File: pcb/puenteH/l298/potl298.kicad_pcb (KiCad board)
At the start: 2 copper layers, 51.1 x 74.4 mm, 19 parts, among them K1 CONN_3, K2 CONN_3, P1 CONN_2X2, P2 v10, P3 CONN_2, P4 CONN_2, U1 L298

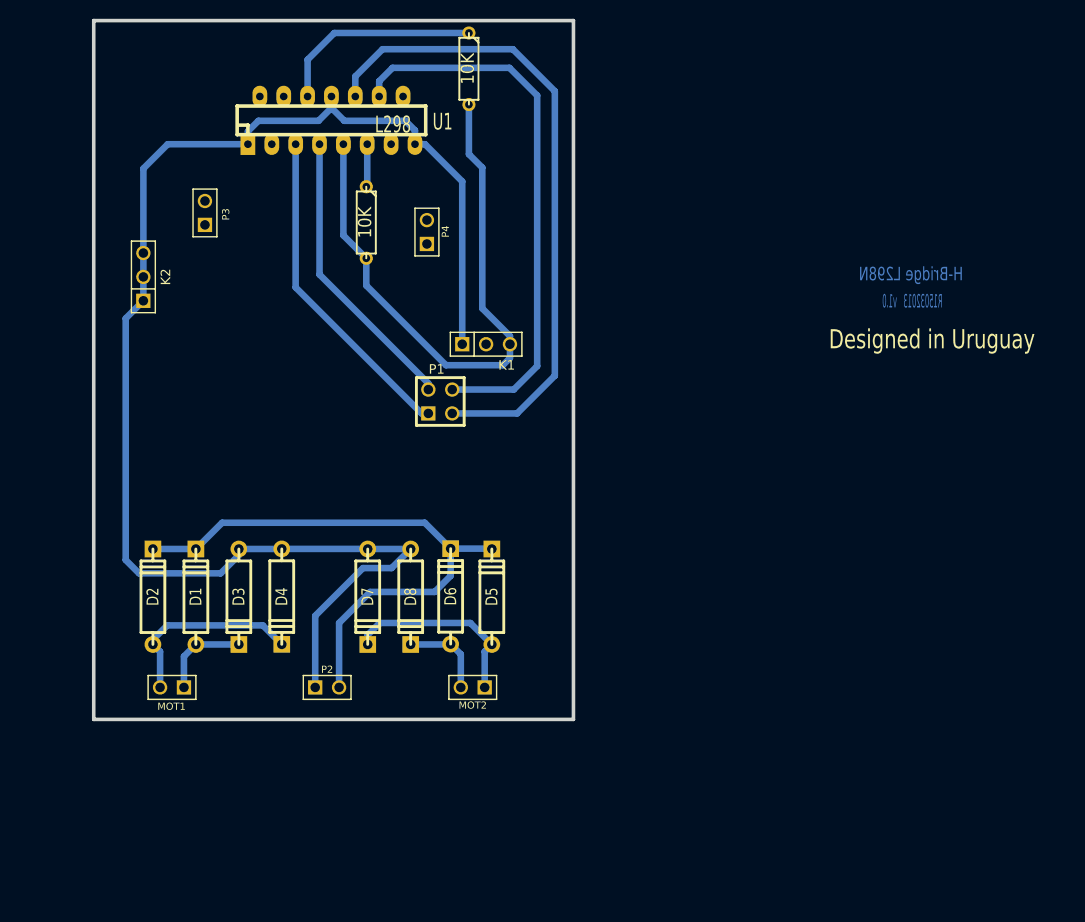
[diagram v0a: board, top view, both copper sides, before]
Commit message: H bridge L298 completed for connect to usb4butia (version 1.8.9 and futures)
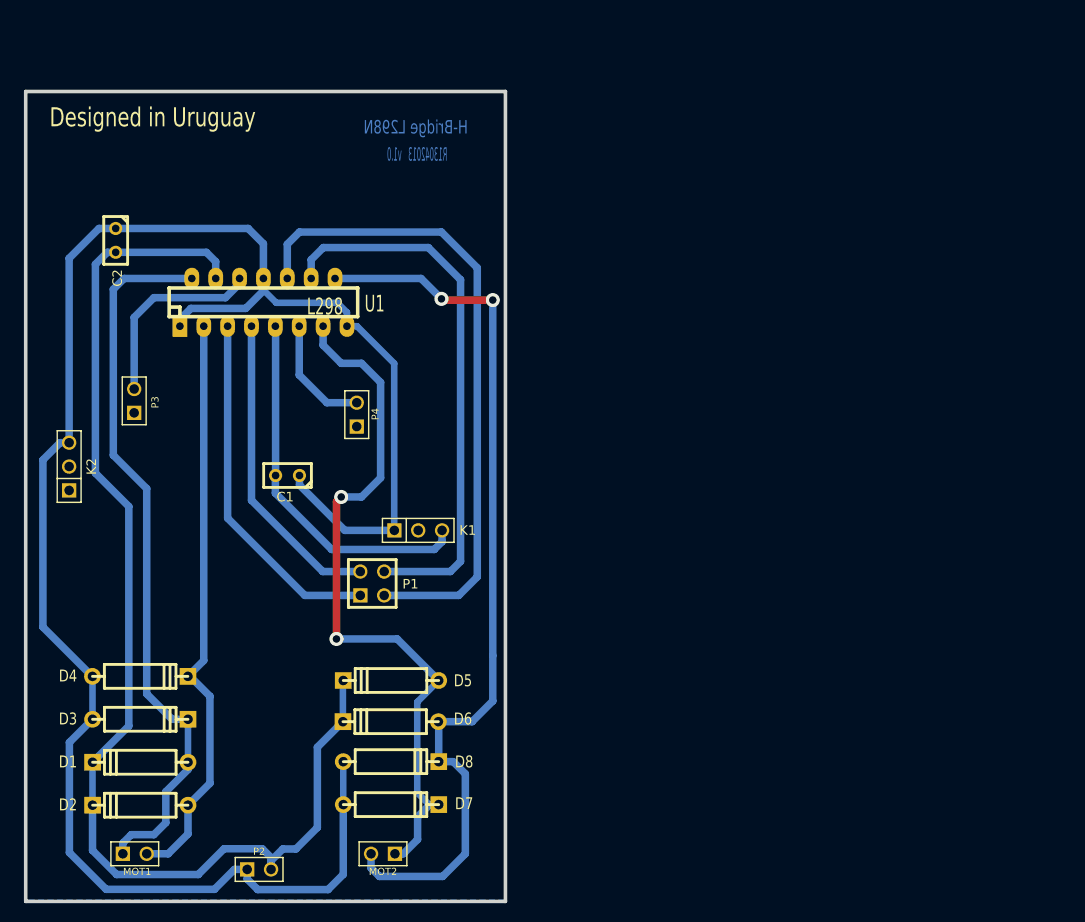
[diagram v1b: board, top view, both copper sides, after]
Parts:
- removed R1, R2: 10K, R3
- added C1: 100nF, C1, F.Cu at (145.3, 95.8)
- added C2: 100nF, C1, F.Cu at (127.0, 70.7)
- P2: value v10 -> PWR
- moved D7 22.3 mm to (156.3, 130.8), turned to 0 degrees
- moved D2 22.2 mm to (129.6, 130.8), turned to 180 degrees
- moved K2 21.7 mm to (122.0, 94.8)
- moved P3 21.4 mm to (129.0, 87.8)
- moved K1 21.1 mm to (159.2, 101.6)
- moved P4 20.8 mm to (152.7, 89.3)
- moved P2 20.7 mm to (142.3, 137.7)
- moved P1 20.7 mm to (154.3, 107.3)
- moved U1 20.7 mm to (142.7, 77.3)
- moved MOT2 20.1 mm to (155.4, 136.0)
- moved D1 18.6 mm to (129.6, 126.3), turned to 180 degrees
- moved MOT1 18.1 mm to (129.0, 136.0), turned to 0 degrees
- moved D8 17.7 mm to (156.3, 126.2), turned to 0 degrees
- moved D4 17.3 mm to (129.6, 117.1), turned to 0 degrees
- moved D3 16.7 mm to (129.6, 121.7), turned to 0 degrees
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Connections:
- net N-0000015 renamed OUT4
- net N-0000016 renamed OUT2
- net N-0000017 renamed OUT1
- net N-0000018 renamed OUT3
- net VCC renamed Vcc
- net VCC_10 renamed Vcc_12
- K2 pad 1: GND -> (no net)
- K2 pad 2: GND -> (no net)
- P3 pad 2: (no net) -> EnA
- P4 pad 2: (no net) -> EnB
- U1 pad 11: N-0000013 -> EnB
- U1 pad 6: N-000005 -> EnA
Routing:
- net OUT4: track 9.30 -> 96.2 mm, vias 0 -> 2
- net OUT1: track 9.67 -> 77.5 mm
- net Vcc_12: track 62.1 -> 127.9 mm
- net OUT3: track 20.6 -> 77.0 mm, vias 0 -> 2
- net GND: track 156.8 -> 203.4 mm
- net OUT2: track 20.6 -> 62.1 mm
- net Vcc: track 64.0 -> 39.6 mm
- net N-000005: track 22.3 -> 0.00 mm
- net EnA: track 0.00 -> 20.9 mm
- net EnB: track 0.00 -> 12.5 mm
- net N-0000013: track 4.56 -> 0.00 mm
- net IN1: track 34.9 -> 38.0 mm
- net IN2: track 30.9 -> 33.3 mm
- net IN4: track 59.1 -> 58.4 mm
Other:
- board size 51.1 x 74.4 mm -> 51.1 x 86.2 mm
- net class Default: trace_width 0.7 -> 0.2032
- rule pad_to_mask_clearance: 0.2 -> 0.254
- rule trace_min: 0.254 -> 0.20066
- rule via_min_drill: 0.508 -> 0.39878
- rule via_min_size: 0.889 -> 0.70104
- board text added: "R13042013 v1.0"
- board text removed: "R15032013 v1.0"
